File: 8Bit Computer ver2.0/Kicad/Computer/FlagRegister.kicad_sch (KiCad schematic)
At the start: 9 parts, among them IC14 SN74HCS4075DR, IC15 SN74AHC08DR, IC27 SN74AHC74DR, IC31 SN74AHC08DR, IC32 SN74AHC74DR, IC36 SN74AHC74DR, IC37 SN74ABT574ADWR, IC4 SN74AHC32DR, IC46 SN74LVC1G14DBVR

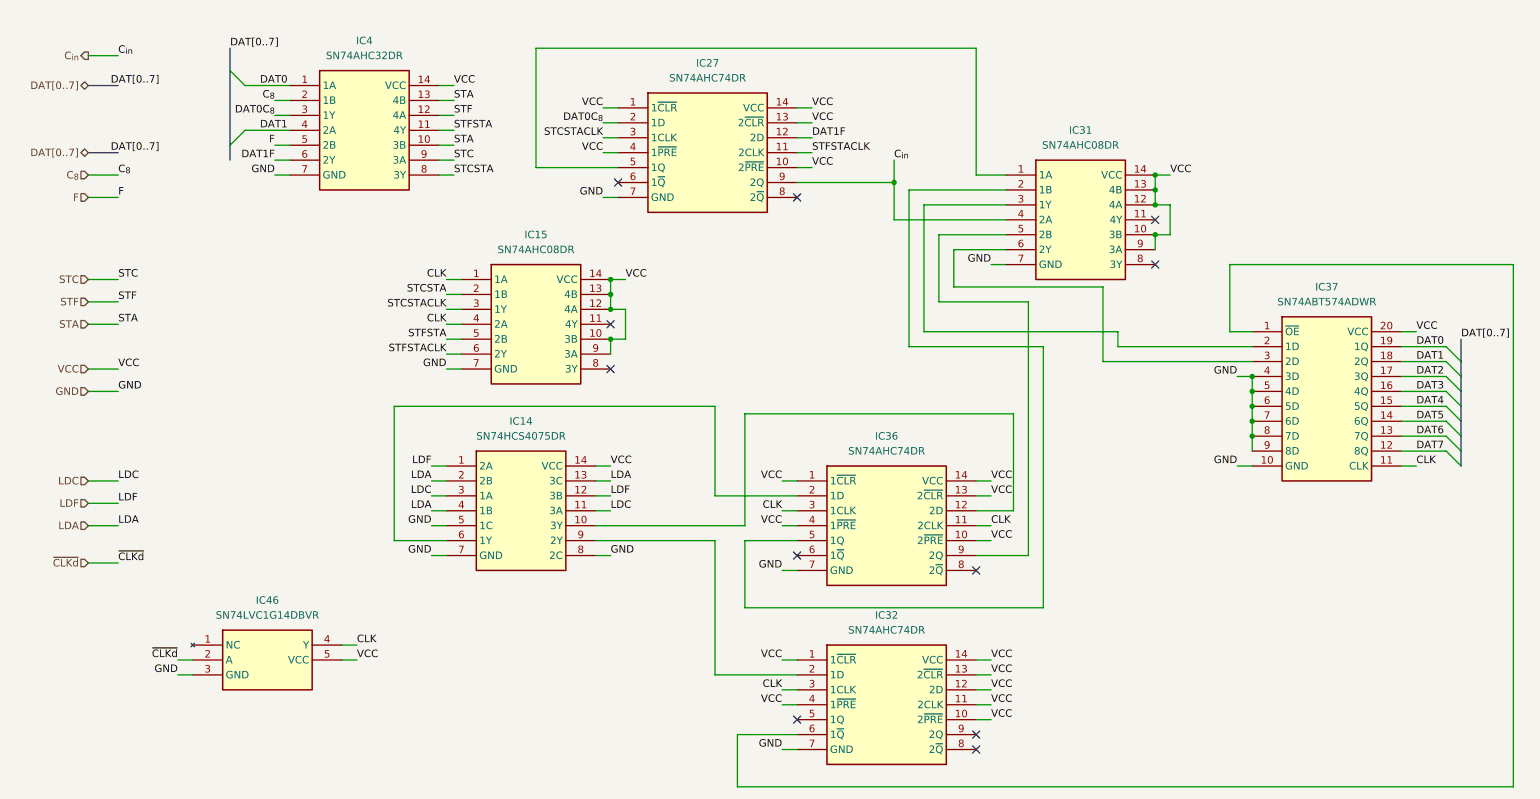
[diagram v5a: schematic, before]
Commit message: Kicad SCH/PCB
Kicad SCH/PCB:
changed the References in SCH
began with INOUTPUT module nearly done
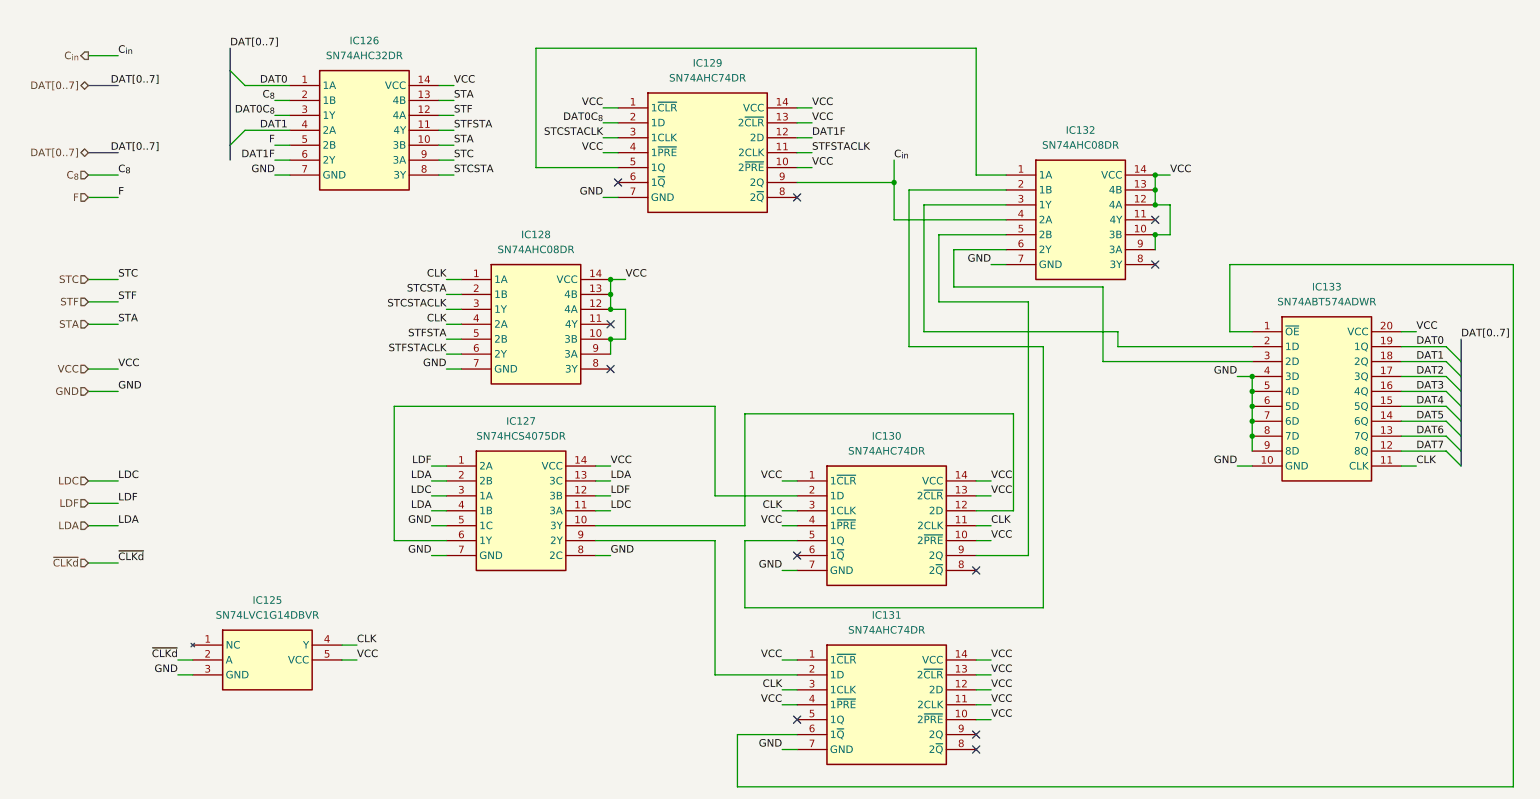
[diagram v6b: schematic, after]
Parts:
- renumbered IC46 to IC125, IC4 to IC126, IC14 to IC127, IC15 to IC128, IC27 to IC129, IC36 to IC130, IC32 to IC131, IC31 to IC132, IC37 to IC133
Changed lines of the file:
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@@
 		(dnp no)
 		(fields_autoplaced yes)
-		(property "Reference" "IC27"
+		(property "Reference" "IC129"
 			(at 137.16 27.94 0)
 			(effects
@@
 			(project ""
 				(path "/1196a00e-6878-4d6d-82b7-9e052dfe7c14/c4d8b530-1c6d-45af-88d2-7dc1d4321a34/b0d3ca8d-4ecf-45d8-adc8-29c6089265db"
-					(reference "IC27")
+					(reference "IC129")
 					(unit 1)
 				)
@@
 		(dnp no)
 		(fields_autoplaced yes)
-		(property "Reference" "IC37"
+		(property "Reference" "IC133"
 			(at 242.57 66.04 0)
 			(effects
@@
 			(project ""
 				(path "/1196a00e-6878-4d6d-82b7-9e052dfe7c14/c4d8b530-1c6d-45af-88d2-7dc1d4321a34/b0d3ca8d-4ecf-45d8-adc8-29c6089265db"
-					(reference "IC37")
+					(reference "IC133")
 					(unit 1)
 				)
@@
 		(dnp no)
 		(fields_autoplaced yes)
-		(property "Reference" "IC36"
+		(property "Reference" "IC130"
 			(at 167.64 91.44 0)
 			(effects
@@
 			(project "Computer"
 				(path "/1196a00e-6878-4d6d-82b7-9e052dfe7c14/c4d8b530-1c6d-45af-88d2-7dc1d4321a34/b0d3ca8d-4ecf-45d8-adc8-29c6089265db"
-					(reference "IC36")
+					(reference "IC130")
 					(unit 1)
 				)
@@
 		(dnp no)
 		(fields_autoplaced yes)
-		(property "Reference" "IC15"
+		(property "Reference" "IC128"
 			(at 107.95 57.15 0)
 			(effects
@@
 			(project ""
 				(path "/1196a00e-6878-4d6d-82b7-9e052dfe7c14/c4d8b530-1c6d-45af-88d2-7dc1d4321a34/b0d3ca8d-4ecf-45d8-adc8-29c6089265db"
-					(reference "IC15")
+					(reference "IC128")
 					(unit 1)
 				)
@@
 		(dnp no)
 		(fields_autoplaced yes)
-		(property "Reference" "IC4"
+		(property "Reference" "IC126"
 			(at 78.74 24.13 0)
 			(effects
@@
 			(project ""
 				(path "/1196a00e-6878-4d6d-82b7-9e052dfe7c14/c4d8b530-1c6d-45af-88d2-7dc1d4321a34/b0d3ca8d-4ecf-45d8-adc8-29c6089265db"
-					(reference "IC4")
+					(reference "IC126")
 					(unit 1)
 				)
@@
 		(dnp no)
 		(fields_autoplaced yes)
-		(property "Reference" "IC32"
+		(property "Reference" "IC131"
 			(at 167.64 121.92 0)
 			(effects
@@
 			(project "Computer"
 				(path "/1196a00e-6878-4d6d-82b7-9e052dfe7c14/c4d8b530-1c6d-45af-88d2-7dc1d4321a34/b0d3ca8d-4ecf-45d8-adc8-29c6089265db"
-					(reference "IC32")
+					(reference "IC131")
 					(unit 1)
 				)
@@
 		(dnp no)
 		(fields_autoplaced yes)
-		(property "Reference" "IC31"
+		(property "Reference" "IC132"
 			(at 200.66 39.37 0)
 			(effects
@@
 			(project "Computer"
 				(path "/1196a00e-6878-4d6d-82b7-9e052dfe7c14/c4d8b530-1c6d-45af-88d2-7dc1d4321a34/b0d3ca8d-4ecf-45d8-adc8-29c6089265db"
-					(reference "IC31")
+					(reference "IC132")
 					(unit 1)
 				)
@@
 		(dnp no)
 		(fields_autoplaced yes)
-		(property "Reference" "IC46"
+		(property "Reference" "IC125"
 			(at 62.23 119.38 0)
 			(effects
@@
 			(project ""
 				(path "/1196a00e-6878-4d6d-82b7-9e052dfe7c14/c4d8b530-1c6d-45af-88d2-7dc1d4321a34/b0d3ca8d-4ecf-45d8-adc8-29c6089265db"
-					(reference "IC46")
+					(reference "IC125")
 					(unit 1)
 				)
@@
 		(dnp no)
 		(fields_autoplaced yes)
-		(property "Reference" "IC14"
+		(property "Reference" "IC127"
 			(at 105.41 88.9 0)
 			(effects
@@
 			(project ""
 				(path "/1196a00e-6878-4d6d-82b7-9e052dfe7c14/c4d8b530-1c6d-45af-88d2-7dc1d4321a34/b0d3ca8d-4ecf-45d8-adc8-29c6089265db"
-					(reference "IC14")
+					(reference "IC127")
 					(unit 1)
 				)

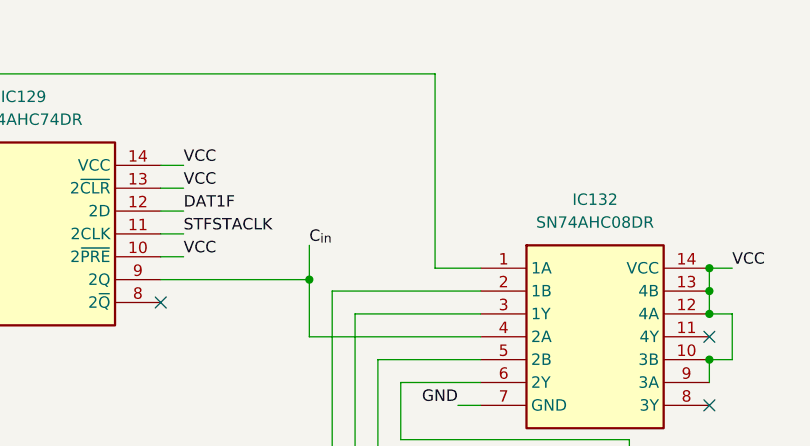
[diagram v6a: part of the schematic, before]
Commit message: Kicad, parts
parts:
added Mux 4:1 for CLK
added LM555
Kicad:
added some Diodes for Flash disable
fixed wrong routing of flag register
fixed wrong routing of STC STF in INC/AddS
LM555 circuit for 1Hz to 100Hz
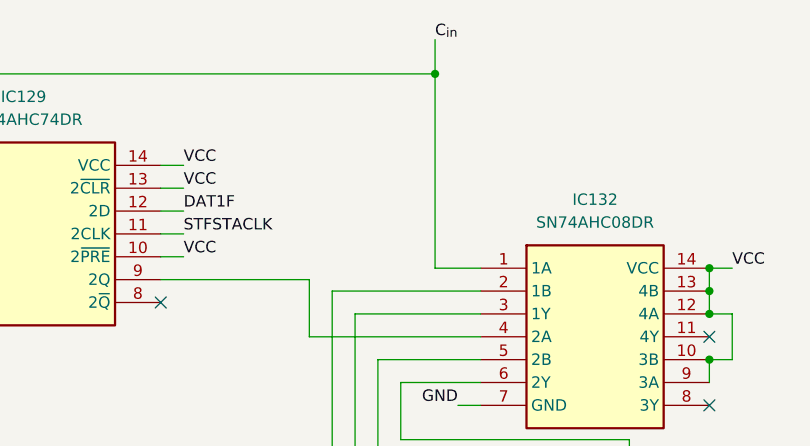
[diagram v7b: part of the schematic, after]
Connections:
- net C_{in}: now also IC129.5 (1Q), IC132.1 (1A); no longer IC129.9 (2Q), IC132.4 (2A)
- new net: IC129.9 (2Q), IC132.4 (2A)
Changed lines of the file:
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@@
+	)
+	(junction
+		(at 182.88 25.4)
+		(diameter 0)
+		(color 0 0 0 0)
 	)
 	(junction
@@
 	)
 	(junction
-		(at 168.91 48.26)
-		(diameter 0)
-		(color 0 0 0 0)
-	)
-	(junction
 		(at 229.87 86.36)
 		(diameter 0)
@@
 	(wire
 		(pts
-			(xy 168.91 44.45) (xy 168.91 48.26)
-		)
-		(stroke
-			(width 0)
-			(type default)
-		)
-	)
-	(wire
-		(pts
 			(xy 92.71 64.77) (xy 95.25 64.77)
 		)
@@
 		(pts
 			(xy 90.17 96.52) (xy 92.71 96.52)
+		)
+		(stroke
+			(width 0)
+			(type default)
+		)
+	)
+	(wire
+		(pts
+			(xy 182.88 21.59) (xy 182.88 25.4)
 		)
 		(stroke
@@
 		)
 	)
-	(label "C_{in}"
-		(at 168.91 44.45 0)
-		(effects
-			(font
-				(size 1.27 1.27)
-			)
-			(justify left bottom)
-		)
-	)
 	(label "STCSTA"
 		(at 93.98 46.99 0)
@@
 		(effects
 			(font
+				(size 1.27 1.27)
+			)
+			(justify left bottom)
+		)
+	)
+	(label "C_{in}"
+		(at 182.88 21.59 0)
+		(effects
+			(font

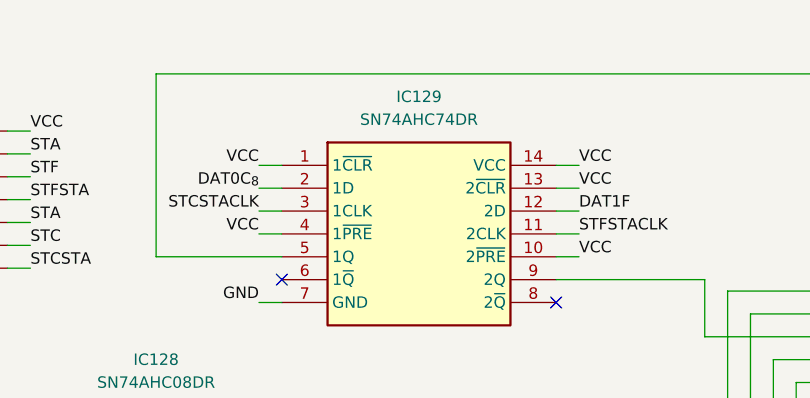
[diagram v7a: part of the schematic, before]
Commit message: Kicad,parts
parts:
added 1N4148 Diode SMD
Kicad:
fixed some routings of Schematic
created Flash mem and RAM PCB
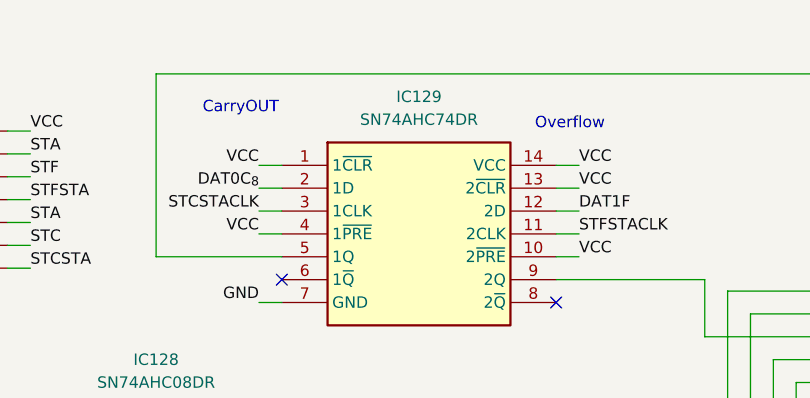
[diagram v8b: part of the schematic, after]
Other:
- note added: "CarryOUT"
- note added: "Overflow"
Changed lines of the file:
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@@
 	(generator_version "9.0")
 	(paper "A4")
+	(text "Overflow"
+		(exclude_from_sim no)
+		(at 153.924 30.988 0)
+		(effects
+			(font
+				(size 1.27 1.27)
+			)
+		)
+	)
+	(text "CarryOUT"
+		(exclude_from_sim no)
+		(at 117.348 29.21 0)
+		(effects
+			(font
+				(size 1.27 1.27)
+			)
+		)
+	)
 	(junction
 		(at 213.36 52.07)
